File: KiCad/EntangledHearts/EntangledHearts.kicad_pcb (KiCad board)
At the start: 2 copper layers, 65 parts

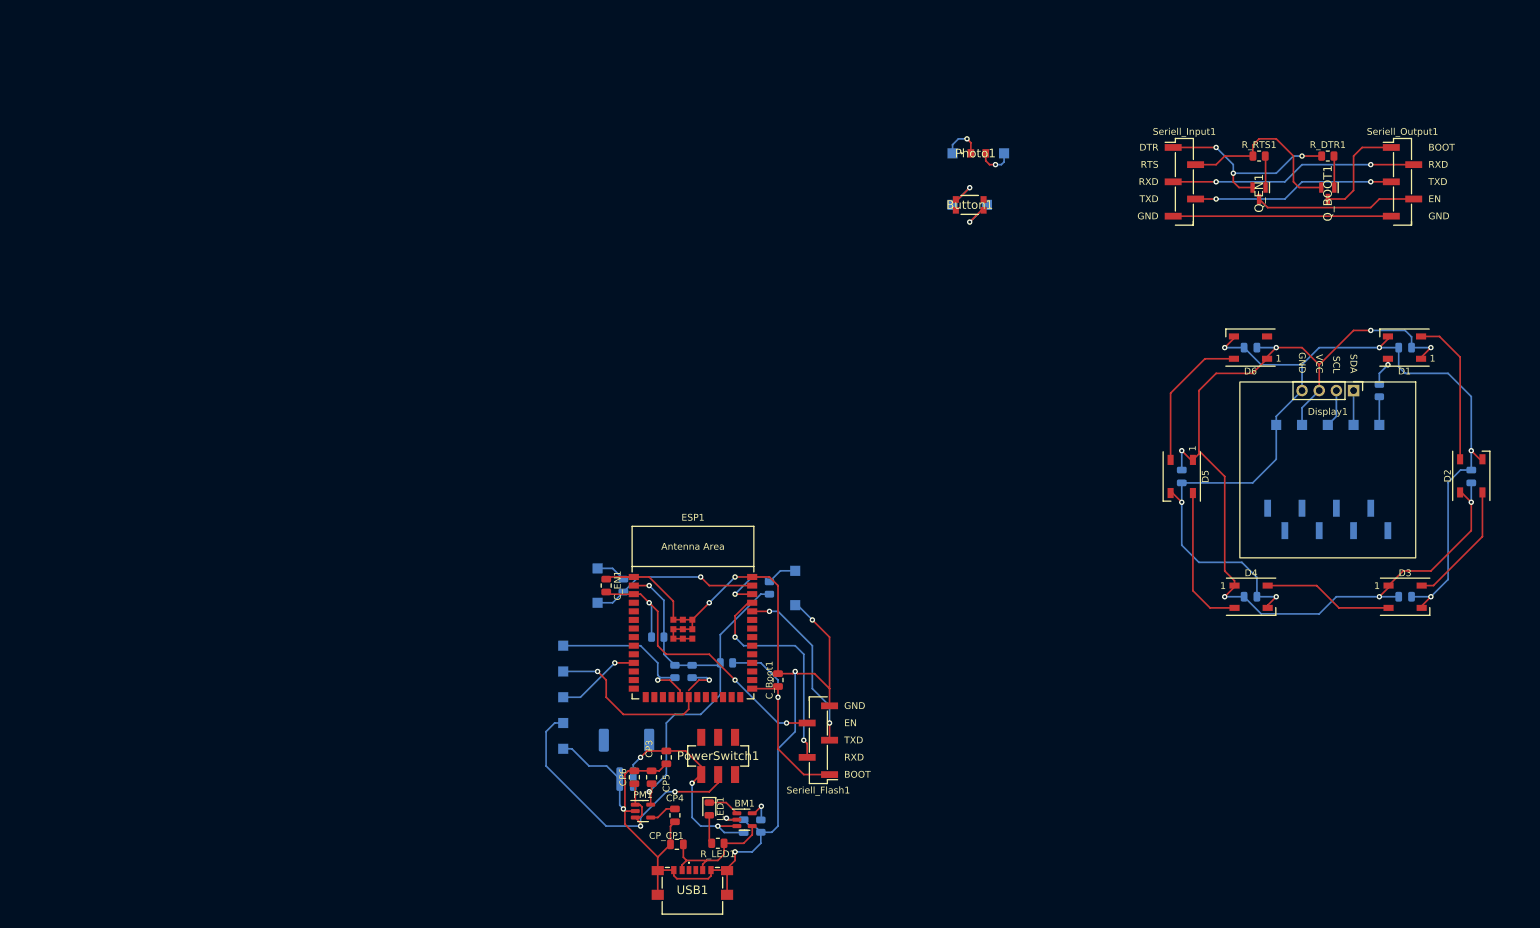
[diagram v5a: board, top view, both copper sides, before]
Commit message: ADD: all errors in PCB fixed
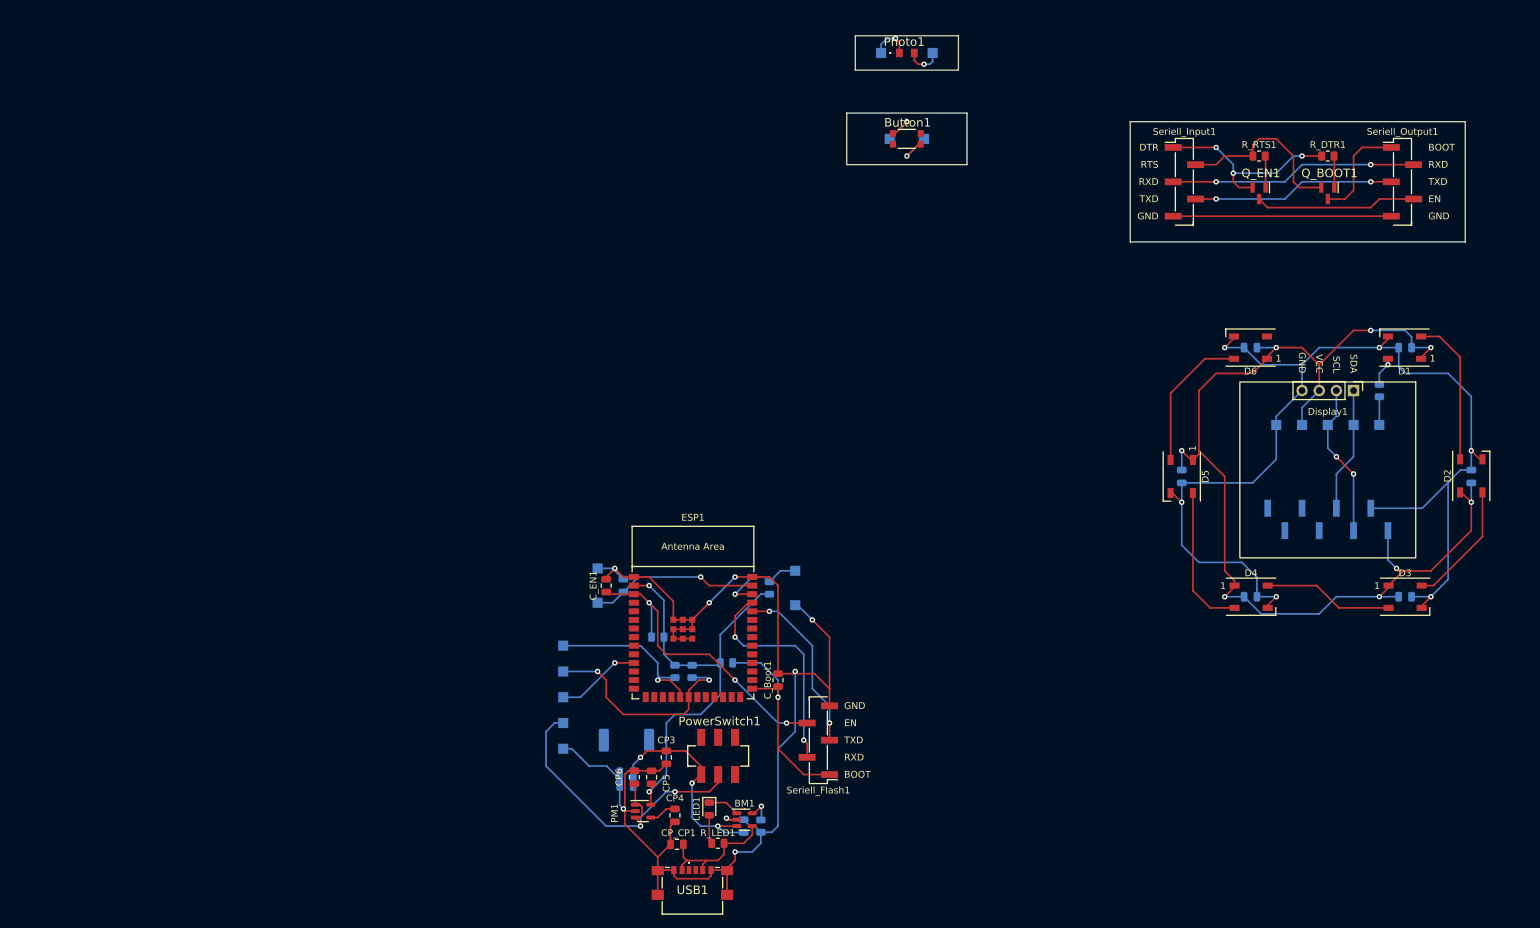
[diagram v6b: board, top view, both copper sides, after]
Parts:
- moved Photo1 18.2 mm to (152.4, 25.4)
- moved PhotoA2 18.2 mm to (156.2, 25.4)
- moved PhotoB2 18.2 mm to (148.6, 25.4)
- moved Button1 13.5 mm to (152.4, 38.1)
- moved ButtonA2 13.5 mm to (149.9, 38.1)
- moved ButtonB2 13.5 mm to (154.9, 38.1)
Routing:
- net SCL_Top: track 5.61 -> 22.8 mm, vias 0 -> 2
- net SDA_Top: track 5.08 -> 18.5 mm
- net GND_Top: track 151.2 -> 164.2 mm
- net VCC_Top: track 152.3 -> 159.5 mm, vias 7 -> 8
- net SCL_Bottom: track 31.1 -> 32.1 mm
- net GND: track 196.6 -> 196.0 mm, vias 7 -> 8
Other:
- board outline added: 91.4 x 30.5 mm
